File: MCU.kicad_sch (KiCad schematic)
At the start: 40 parts, among them J15 Conn_01x08, J16 Conn_02x04_Odd_Even, J17 Conn_01x04_MountingPin, J19 Conn_01x04_MountingPin, SW1 SW_Push_Dual, SW2 SW_Push_Dual, SW3 SW_DIP_x08, U15 MCP1700-3302E_SOT23, U16 CD74HC4067M, U17 MCP2562FD, U18 W25Q256JV, U19 STM32G474MET3, U20 CD74HC4067M, X1 TXC-7C

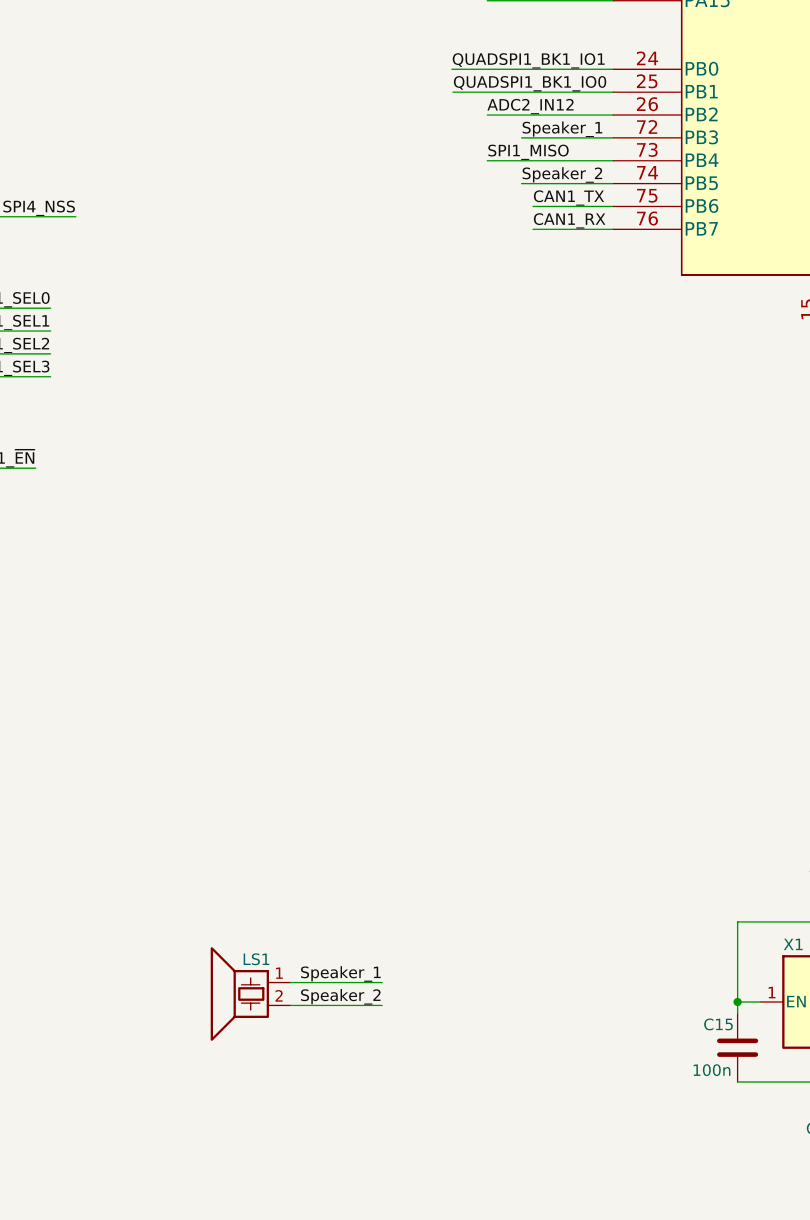
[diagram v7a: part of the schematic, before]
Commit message: Speaker changed to MOSFET circuit
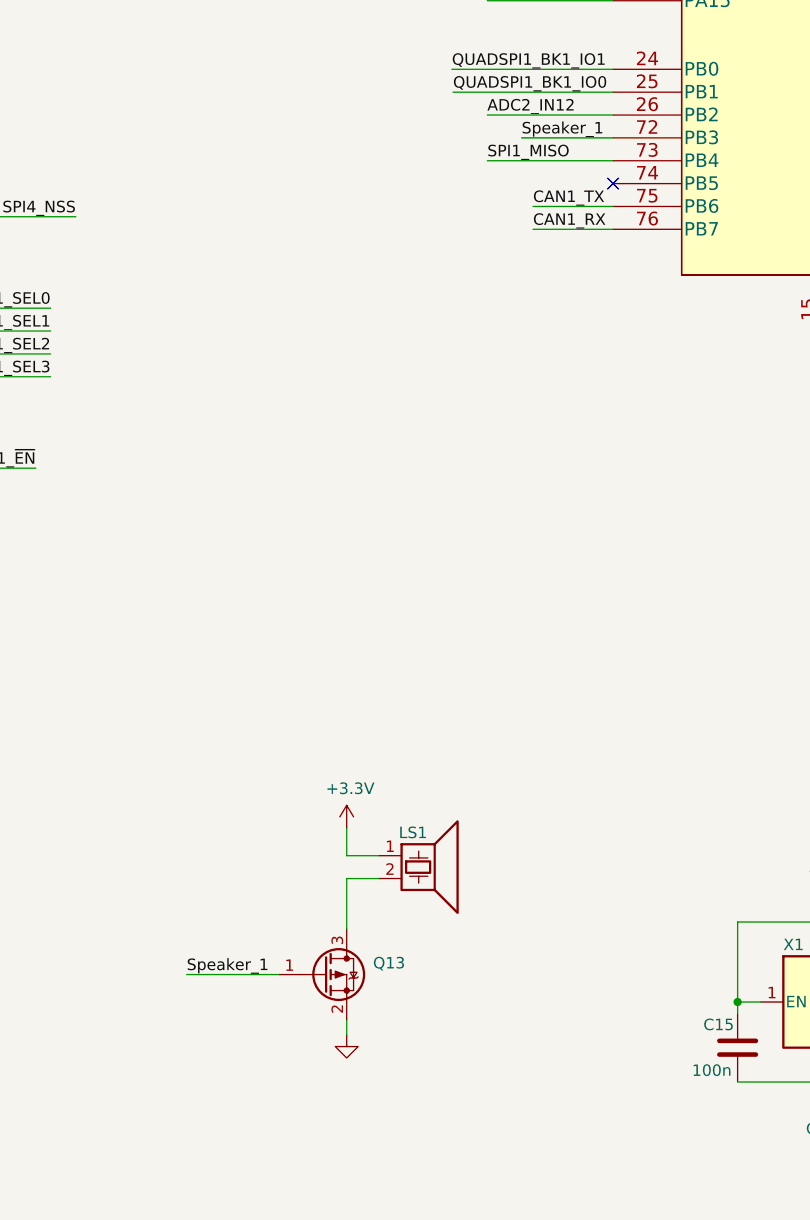
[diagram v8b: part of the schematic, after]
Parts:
- added Q13: (no value), symbol TXV_Library_Symbols:SI2300
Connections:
- net +3V3: now also LS1.1
- net GNDA: now also Q13.2 (S)
- net Speaker_1: now also Q13.1 (G); no longer LS1.1
- net Speaker_2: no longer names the net of LS1.2
- net Speaker_2: now also Q13.3 (D); no longer U19.74 (PB5)
- no-connect marks 15 -> 16
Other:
- moved on the sheet: LS1
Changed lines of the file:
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@@
   (no_connect (at 58.293 85.979))
   (no_connect (at 310.261 126.238))
+  (no_connect (at 239.141 166.878))
   (no_connect (at 141.478 130.048))
   (no_connect (at 141.478 127.508))
@@
     (stroke (width 0) (type default) (color 0 0 0 0))
   )
+  (wire (pts (xy 209.55 238.506) (xy 209.55 241.554))
+    (stroke (width 0) (type default) (color 0 0 0 0))
+  )
   (wire (pts (xy 372.491 112.776) (xy 386.461 112.776))
     (stroke (width 0) (type default) (color 0 0 0 0))
@@
     (stroke (width 0) (type default) (color 0 0 0 0))
   )
-  (wire (pts (xy 203.327 255.651) (xy 213.487 255.651))
+  (wire (pts (xy 201.93 254.762) (xy 191.77 254.762))
     (stroke (width 0) (type default) (color 0 0 0 0))
   )
@@
     (stroke (width 0) (type default) (color 0 0 0 0))
   )
-  (wire (pts (xy 203.327 258.191) (xy 213.487 258.191))
-    (stroke (width 0) (type default) (color 0 0 0 0))
-  )
   (wire (pts (xy 265.811 55.88) (xy 265.811 57.404))
     (stroke (width 0) (type default) (color 0 0 0 0))
@@
     (stroke (width 0) (type default) (color 0 0 0 0))
   )
-  (wire (pts (xy 239.141 166.878) (xy 228.981 166.878))
-    (stroke (width 0) (type default) (color 0 0 0 0))
-  )
   (wire (pts (xy 46.228 262.128) (xy 39.878 262.128))
     (stroke (width 0) (type default) (color 0 0 0 0))
@@
     (stroke (width 0) (type default) (color 0 0 0 0))
   )
+  (wire (pts (xy 209.55 259.842) (xy 209.55 261.493))
+    (stroke (width 0) (type default) (color 0 0 0 0))
+  )
   (wire (pts (xy 132.969 39.751) (xy 138.811 39.751))
     (stroke (width 0) (type default) (color 0 0 0 0))
@@
     (stroke (width 0) (type default) (color 0 0 0 0))
   )
+  (wire (pts (xy 209.55 244.094) (xy 209.55 249.682))
+    (stroke (width 0) (type default) (color 0 0 0 0))
+  )
   (wire (pts (xy 235.204 76.708) (xy 235.204 75.438))
     (stroke (width 0) (type default) (color 0 0 0 0))
@@
     (stroke (width 0) (type default) (color 0 0 0 0))
   )
+  (wire (pts (xy 213.106 244.094) (xy 209.55 244.094))
+    (stroke (width 0) (type default) (color 0 0 0 0))
+  )
   (wire (pts (xy 113.157 188.341) (xy 113.157 185.801))
     (stroke (width 0) (type default) (color 0 0 0 0))
@@
     (stroke (width 0) (type default) (color 0 0 0 0))
   )
+  (wire (pts (xy 209.55 241.554) (xy 213.106 241.554))
+    (stroke (width 0) (type default) (color 0 0 0 0))
+  )
   (wire (pts (xy 150.749 39.751) (xy 156.464 39.751))
     (stroke (width 0) (type default) (color 0 0 0 0))
@@
     (effects (font (size 1.27 1.27)) (justify left bottom))
   )
-  (label "Speaker_1" (at 213.487 255.651 180)
-    (effects (font (size 1.27 1.27)) (justify right bottom))
+  (label "Speaker_1" (at 191.77 254.762 0)
+    (effects (font (size 1.27 1.27)) (justify left bottom))
   )
   (label "GPIO21" (at 372.491 135.509 0)
@@
     (effects (font (size 1.27 1.27)) (justify right bottom))
   )
-  (label "Speaker_2" (at 228.981 166.878 0)
-    (effects (font (size 1.27 1.27)) (justify left bottom))
-  )
   (label "ADC1_IN2" (at 372.618 57.531 0)
     (effects (font (size 1.27 1.27)) (justify left bottom))
@@
   (label "ADC1_IN14" (at 372.618 75.311 0)
     (effects (font (size 1.27 1.27)) (justify left bottom))
-  )
-  (label "Speaker_2" (at 213.487 258.191 180)
-    (effects (font (size 1.27 1.27)) (justify right bottom))
   )
   (label "GPIO10" (at 141.478 114.808 180)
@@
     (pin "1")
     (pin "2")
+  )
+  (symbol (lib_id "power:GNDA") (at 209.55 261.493 0) (unit 1)
+    (in_bom yes) (on_board yes) (fields_autoplaced)
+    (property "Reference" "#PWR0143" (id 0) (at 209.55 267.843 0)
+      (effects (font (size 1.27 1.27)) hide)
+    )
+    (property "Value" "" (id 1) (at 209.55 266.573 0))
+    (property "Footprint" "" (id 2) (at 209.55 261.493 0)
+      (effects (font (size 1.27 1.27)) hide)
+    )
+    (property "Datasheet" "" (id 3) (at 209.55 261.493 0)
+      (effects (font (size 1.27 1.27)) hide)
+    )
+    (pin "1")
   )
   (symbol (lib_id "Switch:SW_Push") (at 46.736 54.864 0) (unit 1)
@@
     (pin "2")
   )
+  (symbol (lib_id "TXV_Library_Symbols:SI2300") (at 207.01 254.762 0) (unit 1)
+    (in_bom yes) (on_board yes) (fields_autoplaced)
+    (property "Reference" "Q13" (id 0) (at 212.471 253.4919 0)
+      (effects (font (size 1.27 1.27)) (justify left))
+    )
+    (property "Value" "" (id 1) (at 212.471 256.0319 0)
+      (effects (font (size 1.27 1.27)) (justify left))
+    )
+    (property "Footprint" "" (id 2) (at 212.09 256.667 0)
+      (effects (font (size 1.27 1.27) italic) (justify left) hide)
+    )
+    (property "Datasheet" "https://www.vishay.com/docs/65701/si2300ds.pdf" (id 3) (at 207.01 254.762 0)
+      (effects (font (size 1.27 1.27)) (justify left) hide)
+    )
+    (pin "1")
+    (pin "2")
+    (pin "3")
+  )
   (symbol (lib_id "power:+5V") (at 58.928 243.078 0) (unit 1)
     (in_bom yes) (on_board yes)
@@
     (pin "4")
     (pin "MP")
+  )
+  (symbol (lib_id "power:+3.3V") (at 209.55 238.506 0) (unit 1)
+    (in_bom yes) (on_board yes)
+    (property "Reference" "#PWR0141" (id 0) (at 209.55 242.316 0)
+      (effects (font (size 1.27 1.27)) hide)
+    )
+    (property "Value" "+3.3V" (id 1) (at 209.931 234.1118 0))
+    (property "Footprint" "" (id 2) (at 209.55 238.506 0)
+      (effects (font (size 1.27 1.27)) hide)
+    )
+    (property "Datasheet" "" (id 3) (at 209.55 238.506 0)
+      (effects (font (size 1.27 1.27)) hide)
+    )
+    (pin "1")
   )
   (symbol (lib_id "power:GNDD") (at 39.243 170.307 0) (unit 1)
@@
     (pin "4")
   )
-  (symbol (lib_id "Device:Speaker_Crystal") (at 198.247 255.651 0) (mirror y) (unit 1)
-    (in_bom yes) (on_board yes)
-    (property "Reference" "LS1" (id 0) (at 199.517 253.111 0))
-    (property "Value" "Speaker_Crystal" (id 1) (at 199.1106 249.9106 0)
-      (effects (font (size 1.27 1.27)) hide)
-    )
-    (property "Footprint" "TXV_Library_Footprints:Piezo_Buzzer" (id 2) (at 199.136 256.921 0)
-      (effects (font (size 1.27 1.27)) hide)
-    )
-    (property "Datasheet" "~" (id 3) (at 199.136 256.921 0)
-      (effects (font (size 1.27 1.27)) hide)
-    )
+  (symbol (lib_id "Device:Speaker_Crystal") (at 218.186 241.554 0) (unit 1)
+    (in_bom yes) (on_board yes)
+    (property "Reference" "LS1" (id 0) (at 216.916 239.014 0))
+    (property "Value" "Speaker_Crystal" (id 1) (at 217.3224 235.8136 0)
+      (effects (font (size 1.27 1.27)) hide)
+    )
+    (property "Footprint" "TXV_Library_Footprints:Piezo_Buzzer" (id 2) (at 217.297 242.824 0)
+      (effects (font (size 1.27 1.27)) hide)
+    )
+    (property "Datasheet" "~" (id 3) (at 217.297 242.824 0)
+      (effects (font (size 1.27 1.27)) hide)
+    )
